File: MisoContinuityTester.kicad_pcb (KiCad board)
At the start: 2 copper layers, 150 x 66 mm, 21 parts, among them J10 OUTPUT, J11 OUTPUT, J12 TYPE1, J13 TYPE2, J3 POWER SWITCH, J4 INPUT, J5 INPUT, J6 FAIL, J7 PASS, J8 POWER 5V-12V, J9 START

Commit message: See OneDrive notes - IB
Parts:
- moved G*** 101.7 mm to (193.7, 89.7), turned to -90 degrees
- moved J3 2.27 mm to (77.5, 68.3)
- moved J13 1.40 mm to (127.7, 68.6)
- moved R1 1.20 mm to (85.8, 71.0)
- moved J12 1.10 mm to (120.4, 68.6)
- moved J9 0.83 mm to (113.1, 68.6)
- moved J6 0.50 mm to (100.8, 68.6)
- moved R2 0.30 mm to (105.8, 71.1)
- moved J7 0.27 mm to (93.5, 68.6)
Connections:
- J6 pad 2: /FAIL -> Net-(J6-Pin_2)
- J7 pad 2: /PASS -> Net-(J7-Pin_2)
- R1 pad 1: /PASS -> Net-(J7-Pin_2)
- R1 pad 2: unconnected-(R1-Pad2) -> /PASS
- R2 pad 1: /FAIL -> Net-(J6-Pin_2)
- R2 pad 2: unconnected-(R2-Pad2) -> /FAIL
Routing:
- net GND: track 178.1 -> 0.67 mm
- net /B13: track 205.6 -> 127.1 mm
- net /B14: track 205.1 -> 134.3 mm
- net /B15: track 204.6 -> 141.9 mm
- net +5V: track 114.3 -> 57.0 mm, vias 0 -> 12
- net /B16: track 204.0 -> 149.4 mm
- net /B17: track 202.8 -> 157.1 mm
- net /A19: track 101.6 -> 59.4 mm, vias 0 -> 1
- net /B18: track 202.2 -> 164.6 mm
- net /A12: track 43.6 -> 76.7 mm
- net /A18: track 91.6 -> 59.4 mm, vias 0 -> 1
- net /B19: track 201.6 -> 172.3 mm
- net /A13: track 43.9 -> 72.7 mm
- net /A20: track 85.2 -> 59.4 mm, vias 0 -> 1
- net /A11: track 103.1 -> 80.0 mm
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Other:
- board text added: "18-WIRE"
- board text added: "20-WIRE"
- board text added: "5V-12V"
- board text added: "9-WIRE"
- board text added: "A1"
- board text added: "A10"
- board text added: "A11"
- board text added: "A12"
- board text added: "A13"
- board text added: "A14"
- board text added: "A15"
- board text added: "A16"
- board text added: "A17"
- board text added: "A18"
- board text added: "A19"
- board text added: "A2"
- board text added: "A20"
- board text added: "A3"
- board text added: "A4"
- board text added: "A5"
- board text added: "A6"
- board text added: "A7"
- board text added: "A8"
- board text added: "A9"
- board text added: "B1"
- board text added: "B10"
- board text added: "B11"
- board text added: "B12"
- board text added: "B13"
- board text added: "B14"
- board text added: "B15"
- board text added: "B16"
- board text added: "B17"
- board text added: "B18"
- board text added: "B19"
- board text added: "B2"
- board text added: "B20"
- board text added: "B3"
- board text added: "B4"
- board text added: "B5"
- board text added: "B6"
- board text added: "B7"
- board text added: "B8"
- board text added: "B9"
- board text added: "FAIL +"
- board text added: "FAIL -"
- board text added: "GND"
- board text added: "JUMPER 'PWR A' AND 'PWR B' IF NO POWER SWITCH USED"
- board text added: "PASS +"
- board text added: "PASS -"
- board text added: "PWR A"
- board text added: "PWR B"
- board text added: "VIN"

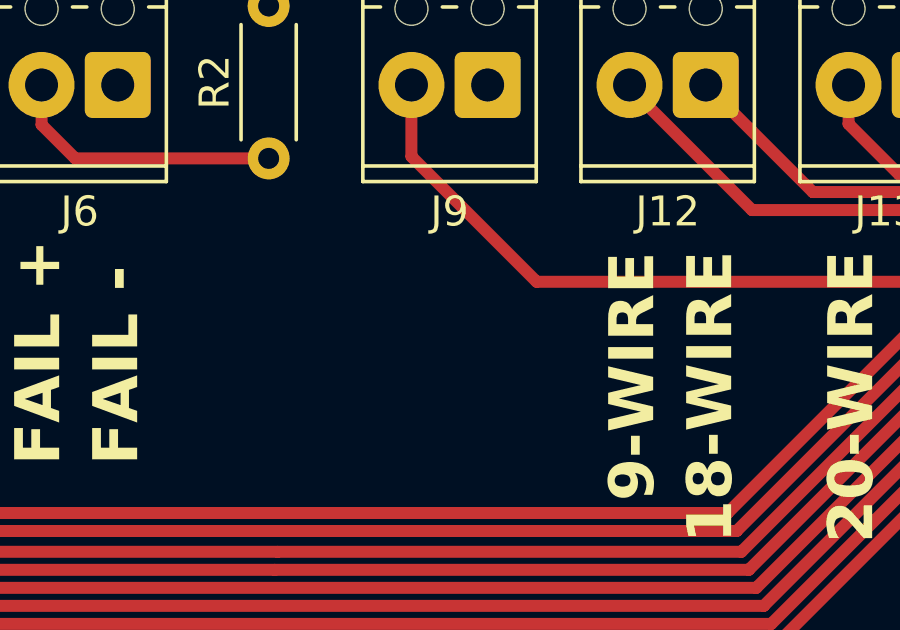
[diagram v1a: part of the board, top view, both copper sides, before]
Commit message: Added 'start' button labels
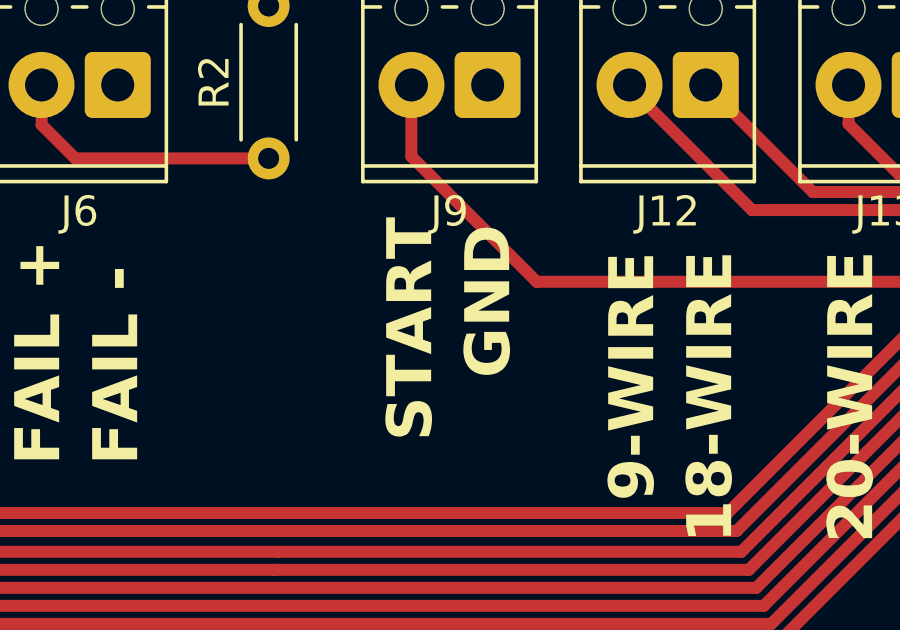
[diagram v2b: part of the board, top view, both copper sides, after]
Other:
- board text added: "START"
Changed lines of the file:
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@@
+		)
+	)
+	(gr_text "START"
+		(at 111.4 80.5 90)
+		(layer "F.SilkS")
+		(effects
+			(font
+				(size 1.5 1.5)
+				(thickness 0.3)
+				(bold yes)
+			)
+			(justify left bottom)
 		)
 	)
@@
 		(layer "F.SilkS")
 		(effects
+			(font
+				(size 1.5 1.5)
+				(thickness 0.3)
+				(bold yes)
+			)
+			(justify left bottom)
+		)
+	)
+	(gr_text "GND"
+		(at 114 78.4 90)
+		(layer "F.SilkS")
+		(effects
